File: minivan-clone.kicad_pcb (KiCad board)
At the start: 2 copper layers, 247.4 x 75.9 mm, 122 parts, among them CON101 HRO-TYPE-C-31-M-12, K101 KEYSW, K102 KEYSW, K103 KEYSW, K104 KEYSW, K105 KEYSW, K106 KEYSW, K107 KEYSW, K108 KEYSW, K109 KEYSW, K110 KEYSW, K111 KEYSW, K112 KEYSW, K113 KEYSW, K114 KEYSW, K115 KEYSW, K116 KEYSW, K118 KEYSW, K119 KEYSW, K120 KEYSW, K121 KEYSW, K122 KEYSW, K123 KEYSW, K124 KEYSW, K125 KEYSW, K126 KEYSW, K127 KEYSW, K128 KEYSW, K129 KEYSW, K130 KEYSW, K131 KEYSW, K132 KEYSW, K133 KEYSW, K134 KEYSW, K135 KEYSW, K136 KEYSW, K137 KEYSW, K138 KEYSW, K139 KEYSW, K140 KEYSW, K141 KEYSW, K142 KEYSW, K143 KEYSW, K144 KEYSW, K145 KEYSW, K146 KEYSW, K147 KEYSW, K148 KEYSW, SW101 SW_PUSH, U101 ATMEGA32U2, X101 XTAL_GND

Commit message: done with tracks for leftmost cols
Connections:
- >NAME pad 1: /PC4 -> /PD4
- D101 pad 1: /PB0 -> /PB6
- D102 pad 1: /PB0 -> /PB6
- D103 pad 1: /PB0 -> /PB6
- D104 pad 1: /PB0 -> /PB6
- D105 pad 1: /PB0 -> /PB6
- D106 pad 1: /PB0 -> /PB6
- D107 pad 1: /PB0 -> /PB6
- D108 pad 1: /PB0 -> /PB6
- D109 pad 1: /PB0 -> /PB6
- D110 pad 1: /PB0 -> /PB6
- D111 pad 1: /PB0 -> /PB6
- D112 pad 1: /PB0 -> /PB6
- D113 pad 1: /PB0 -> /PB6
- D114 pad 1: /PB1 -> /PB5
- D115 pad 1: /PB1 -> /PB5
- D116 pad 1: /PB1 -> /PB5
- D117 pad 1: /PB1 -> /PB5
- D118 pad 1: /PB1 -> /PB5
- D119 pad 1: /PB1 -> /PB5
- D120 pad 1: /PB1 -> /PB5
- D121 pad 1: /PB1 -> /PB5
- D122 pad 1: /PB1 -> /PB5
- D123 pad 1: /PB1 -> /PB5
- D124 pad 1: /PB1 -> /PB5
- D125 pad 1: /PB1 -> /PB5
- K101 pad 1: /PD6 -> /PC6
- K103 pad 1: /PD5 -> /PB7
- K104 pad 1: /PD4 -> /PC4
- K109 pad 1: /PB5 -> /PB1
- K110 pad 1: /PB6 -> /PB0
- K111 pad 1: /PC6 -> /PD6
- K112 pad 1: /PB7 -> /PD5
- K113 pad 1: /PC4 -> /PD4
- K115 pad 1: /PD5 -> /PB7
- K116 pad 1: /PD4 -> /PC4
- K122 pad 1: /PB5 -> /PB1
- K123 pad 1: /PB6 -> /PB0
- K124 pad 1: /PC6 -> /PD6
- K125 pad 1: /PB7 -> /PD5
- K126 pad 1: /PC4 -> /PD4
- K128 pad 1: /PD5 -> /PB7
- K129 pad 1: /PD4 -> /PC4
- K134 pad 1: /PB5 -> /PB1
- K135 pad 1: /PB6 -> /PB0
- K136 pad 1: /PC6 -> /PD6
- K137 pad 1: /PB7 -> /PD5
- K138 pad 1: /PC4 -> /PD4
- K139 pad 1: /PD5 -> /PB7
- K140 pad 1: /PD4 -> /PC4
- K145 pad 1: /PB5 -> /PB1
- K146 pad 1: /PB6 -> /PB0
- K147 pad 1: /PC6 -> /PD6
- K148 pad 1: /PB7 -> /PD5
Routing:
- net /PB5: track 48.0 -> 218.8 mm, vias 0 -> 2
- net /PD6: track 0.00 -> 162.0 mm, vias 0 -> 1
- net /PB6: track 103.0 -> 237.7 mm, vias 1 -> 2
- net /PC6: track 121.1 -> 0.00 mm, vias 1 -> 0
- net /PB1: track 218.8 -> 124.8 mm, vias 2 -> 1
- net /PB0: track 237.7 -> 144.7 mm, vias 2 -> 1
- net /PD4: track 91.1 -> 172.9 mm
- net /PD5: track 91.1 -> 170.6 mm, vias 0 -> 1
- net /PB2: track 48.0 -> 87.2 mm
- net /PC4: track 122.4 -> 91.1 mm
- net /PB7: track 107.0 -> 91.1 mm, vias 1 -> 0
- net Net-(D134-Pad2): track 0.00 -> 9.69 mm
- net Net-(D136-Pad2): track 0.00 -> 9.69 mm
- net Net-(D135-Pad2): track 0.00 -> 9.59 mm
- net Net-(D133-Pad2): track 0.00 -> 9.59 mm
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
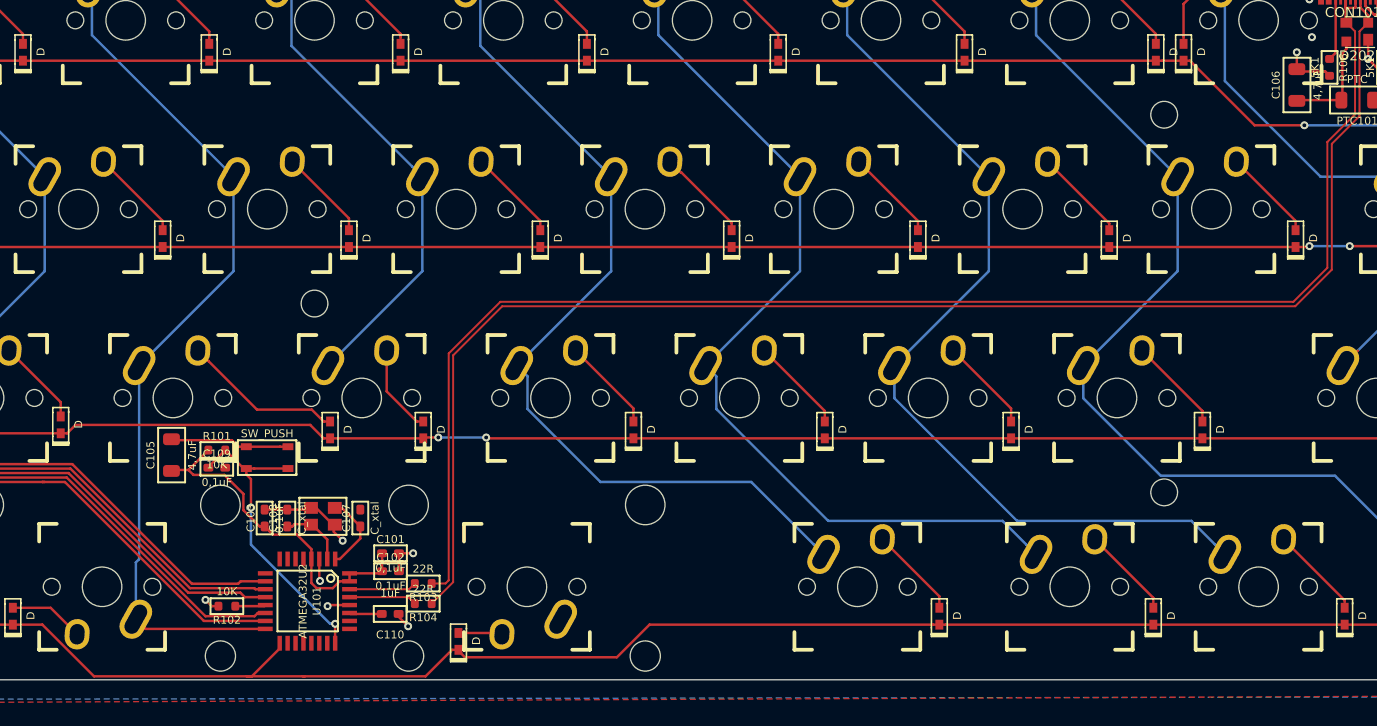
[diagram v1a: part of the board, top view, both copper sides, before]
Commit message: tracks for all leftmost rows, started with rightmost cols
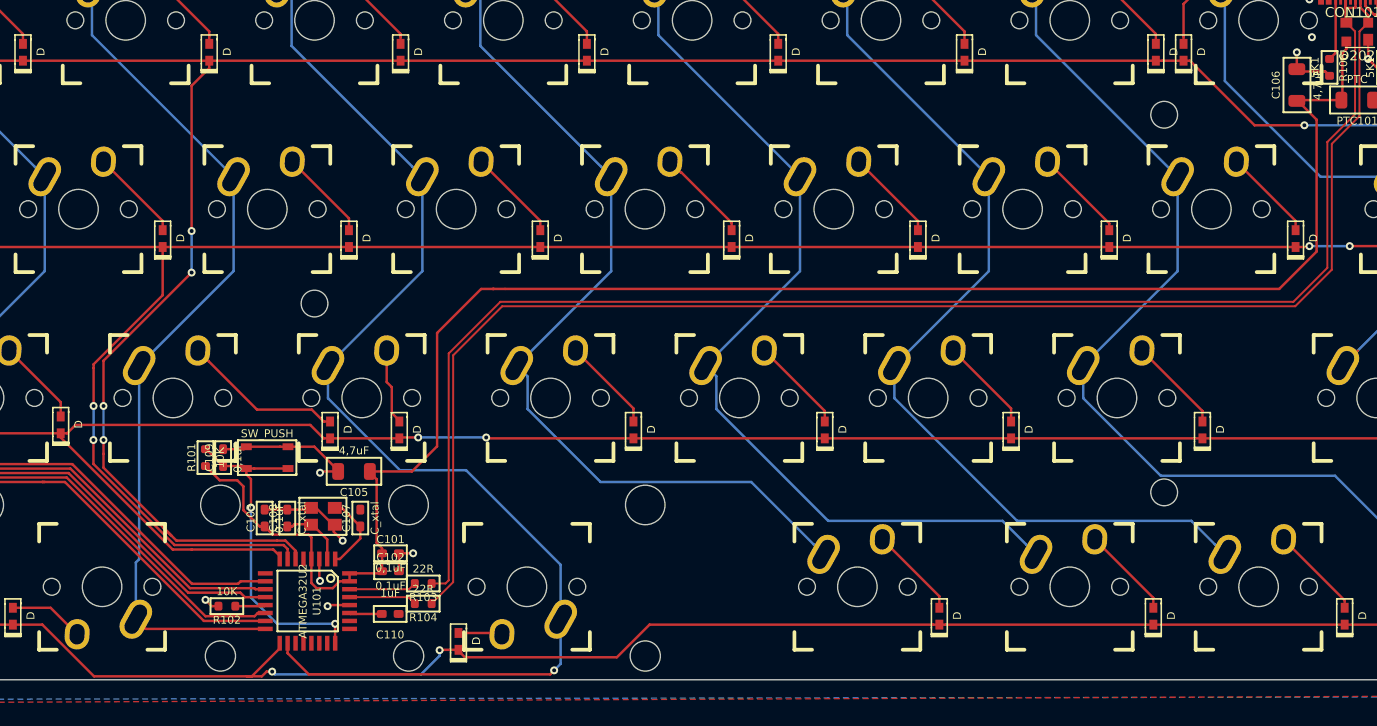
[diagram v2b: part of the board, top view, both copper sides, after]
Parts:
- moved C105 18.5 mm to (248.3, 183.5), turned to 180 degrees
- moved D132 2.41 mm to (252.9, 179.3)
- moved R101 1.37 mm to (233.3, 182.1), turned to 90 degrees
- moved C109 1.20 mm to (235.1, 182.1), turned to 90 degrees
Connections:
- D101 pad 1: /PB6 -> /PD0
- D102 pad 1: /PB6 -> /PD0
- D103 pad 1: /PB6 -> /PD0
- D104 pad 1: /PB6 -> /PD0
- D105 pad 1: /PB6 -> /PD0
- D106 pad 1: /PB6 -> /PD0
- D107 pad 1: /PB6 -> /PD0
- D108 pad 1: /PB6 -> /PD0
- D109 pad 1: /PB6 -> /PD0
- D110 pad 1: /PB6 -> /PD0
- D111 pad 1: /PB6 -> /PD0
- D112 pad 1: /PB6 -> /PD0
- D113 pad 1: /PB6 -> /PD0
- D114 pad 1: /PB5 -> /PD1
- D115 pad 1: /PB5 -> /PD1
- D116 pad 1: /PB5 -> /PD1
- D117 pad 1: /PB5 -> /PD1
- D118 pad 1: /PB5 -> /PD1
- D119 pad 1: /PB5 -> /PD1
- D120 pad 1: /PB5 -> /PD1
- D121 pad 1: /PB5 -> /PD1
- D122 pad 1: /PB5 -> /PD1
- D123 pad 1: /PB5 -> /PD1
- D124 pad 1: /PB5 -> /PD1
- D125 pad 1: /PB5 -> /PD1
- D126 pad 1: /PC2 -> /PD2
- D127 pad 1: /PC2 -> /PD2
- D128 pad 1: /PC2 -> /PD2
- D129 pad 1: /PC2 -> /PD2
- D130 pad 1: /PC2 -> /PD2
- D131 pad 1: /PC2 -> /PD2
- D132 pad 1: /PC2 -> /PD2
- D133 pad 1: /PC2 -> /PD2
- D134 pad 1: /PC2 -> /PD2
- D135 pad 1: /PC2 -> /PD2
- D136 pad 1: /PC2 -> /PD2
- D137 pad 1: /PC2 -> /PD2
- K102 pad 1: /PB4 -> /PB6
- K106 pad 1: /PD2 -> /PC2
- K107 pad 1: /PD0 -> /PB4
- K114 pad 1: /PB4 -> /PB6
- K119 pad 1: /PD2 -> /PC2
- K120 pad 1: /PD0 -> /PB4
- K127 pad 1: /PB4 -> /PB6
- K131 pad 1: /PD2 -> /PC2
- K132 pad 1: /PD0 -> /PB4
- K142 pad 1: /PD2 -> /PC2
- K143 pad 1: /PD0 -> /PB4
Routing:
- net /PD1: track 0.00 -> 267.7 mm, vias 0 -> 4
- net /PD0: track 48.0 -> 308.1 mm, vias 0 -> 6
- net /PB5: track 218.8 -> 0.00 mm, vias 2 -> 0
- net /PB6: track 237.7 -> 53.2 mm, vias 2 -> 0
- net /PD2: track 88.7 -> 248.2 mm, vias 0 -> 2
- net /PC2: track 220.4 -> 88.7 mm, vias 2 -> 0
- net +5V: track 45.7 -> 177.3 mm
- net /PB4: track 53.2 -> 121.6 mm, vias 0 -> 1
- net /RST: track 31.4 -> 34.4 mm
- net GND: track 46.2 -> 47.6 mm
- net Net-(D132-Pad2): track 9.07 -> 7.69 mm
- net /PB3: track 237.0 -> 237.4 mm, vias 0 -> 2

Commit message: added all tracks
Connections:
- K101 pad 1: /PC6 -> /PC7
- K102 pad 1: /PB6 -> /PC6
- K103 pad 1: /PB7 -> /PC4
- K104 pad 1: /PC4 -> /PC5
- K105 pad 1: /PD3 -> /PB6
- K106 pad 1: /PC2 -> /PB5
- K114 pad 1: /PB6 -> /PC6
- K115 pad 1: /PB7 -> /PC4
- K116 pad 1: /PC4 -> /PC5
- K118 pad 1: /PD3 -> /PB6
- K119 pad 1: /PC2 -> /PB5
- K127 pad 1: /PB6 -> /PC6
- K128 pad 1: /PB7 -> /PC4
- K129 pad 1: /PC4 -> /PC5
- K130 pad 1: /PD3 -> /PB6
- K131 pad 1: /PC2 -> /PB5
- K139 pad 1: /PB7 -> /PC4
- K140 pad 1: /PC4 -> /PC5
- K141 pad 1: /PD3 -> /PB6
- K142 pad 1: /PC2 -> /PB5
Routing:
- net /PC5: track 0.00 -> 188.2 mm, vias 0 -> 2
- net /PC7: track 0.00 -> 169.9 mm, vias 0 -> 3
- net /PC6: track 0.00 -> 169.0 mm, vias 0 -> 3
- net /PB5: track 0.00 -> 148.7 mm
- net /PB6: track 53.2 -> 176.8 mm, vias 0 -> 2
- net /PC4: track 91.1 -> 209.6 mm, vias 0 -> 2
- net /PD3: track 91.1 -> 0.00 mm
- net /PB7: track 91.1 -> 0.00 mm
- net /PC2: track 88.7 -> 0.00 mm
- net Net-(D101-Pad2): track 24.1 -> 21.8 mm

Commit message: fixed fills
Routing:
- net /PD6: track 162.0 -> 165.9 mm
- net /RST: track 34.4 -> 30.9 mm
- net /PC7: track 169.9 -> 170.9 mm

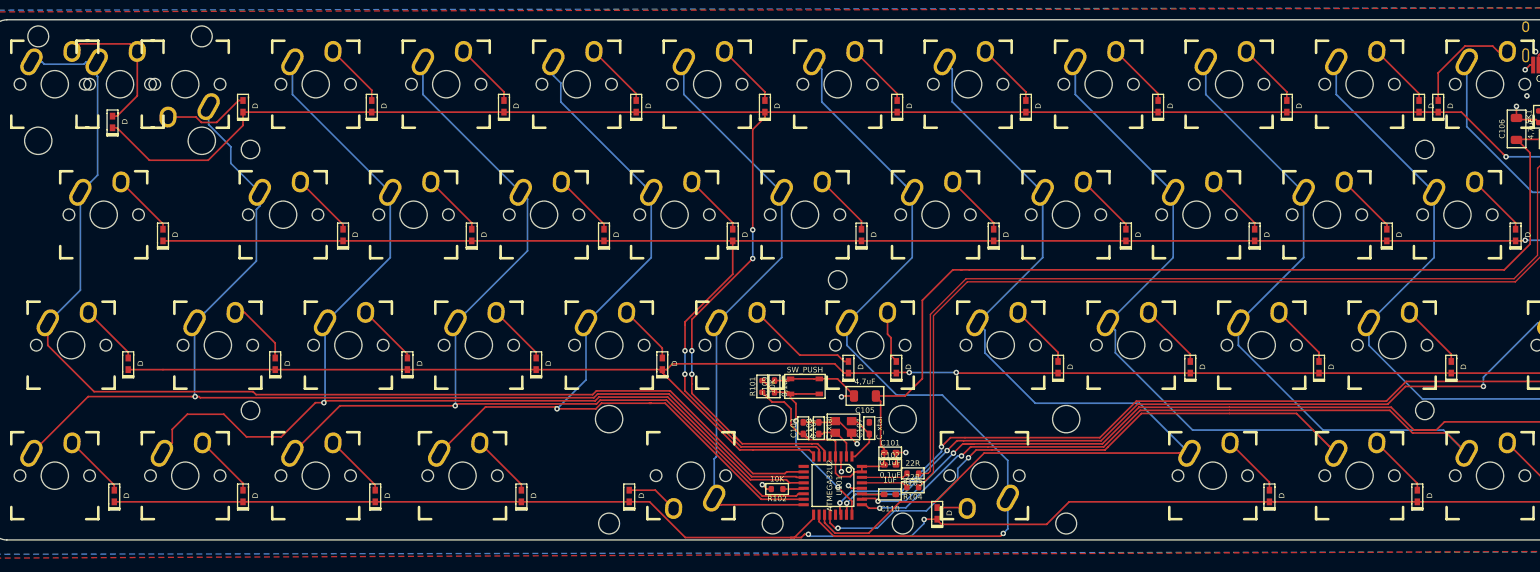
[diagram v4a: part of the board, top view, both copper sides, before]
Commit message: fixed DRC errors
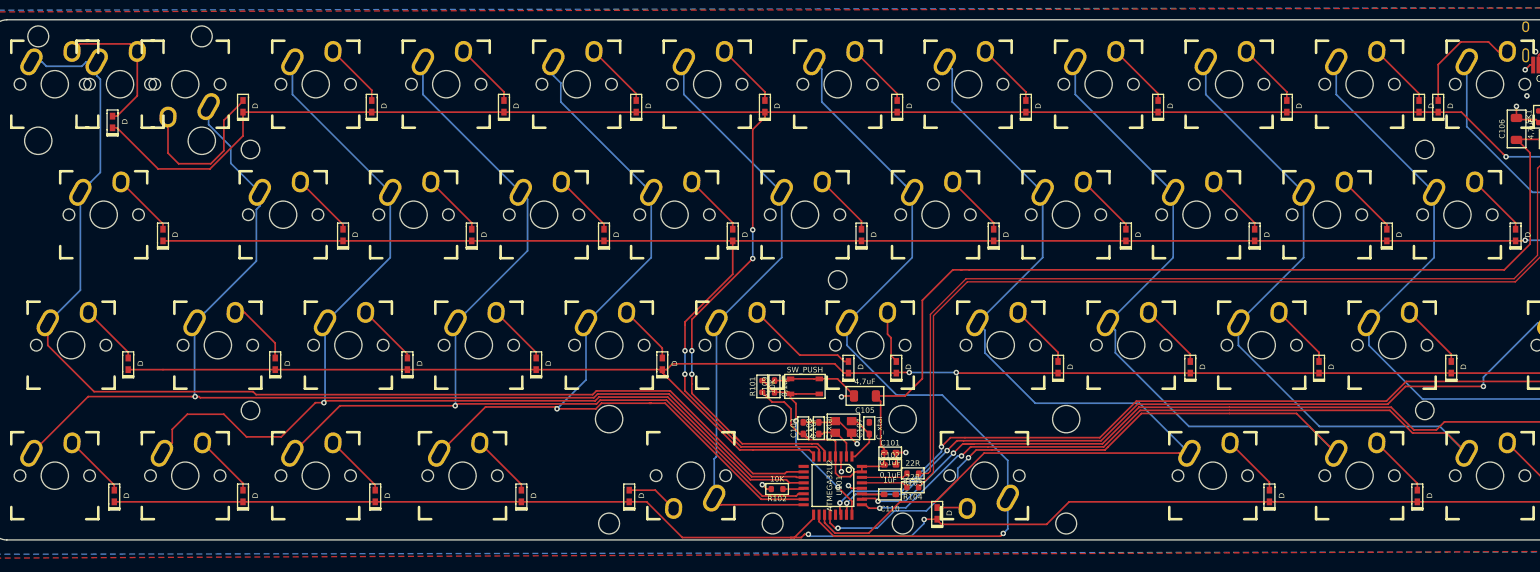
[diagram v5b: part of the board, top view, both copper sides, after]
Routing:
- net Net-(D102-Pad2): track 12.6 -> 23.3 mm
- net /PD0: track 308.1 -> 310.0 mm
- net Net-(D112-Pad2): track 16.1 -> 17.3 mm
- net /PD4: track 172.9 -> 173.5 mm

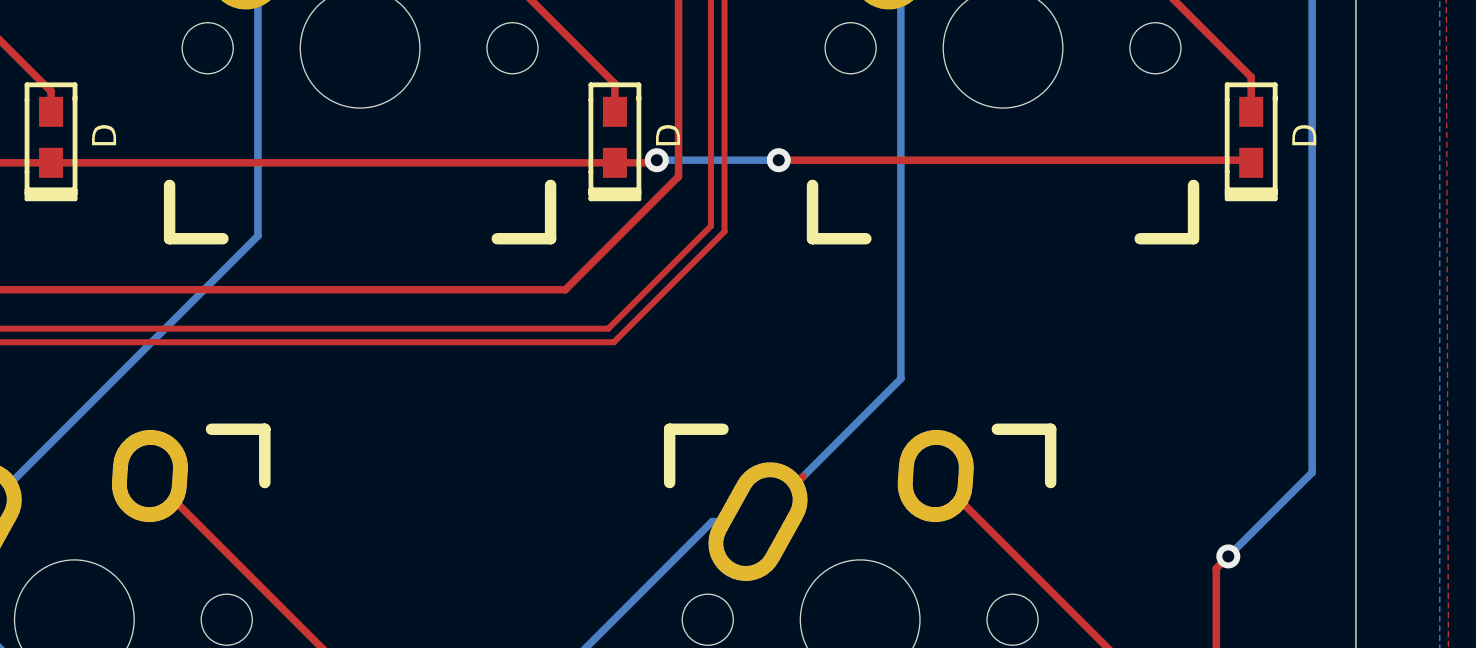
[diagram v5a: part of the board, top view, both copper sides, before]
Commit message: fixed logo in silk
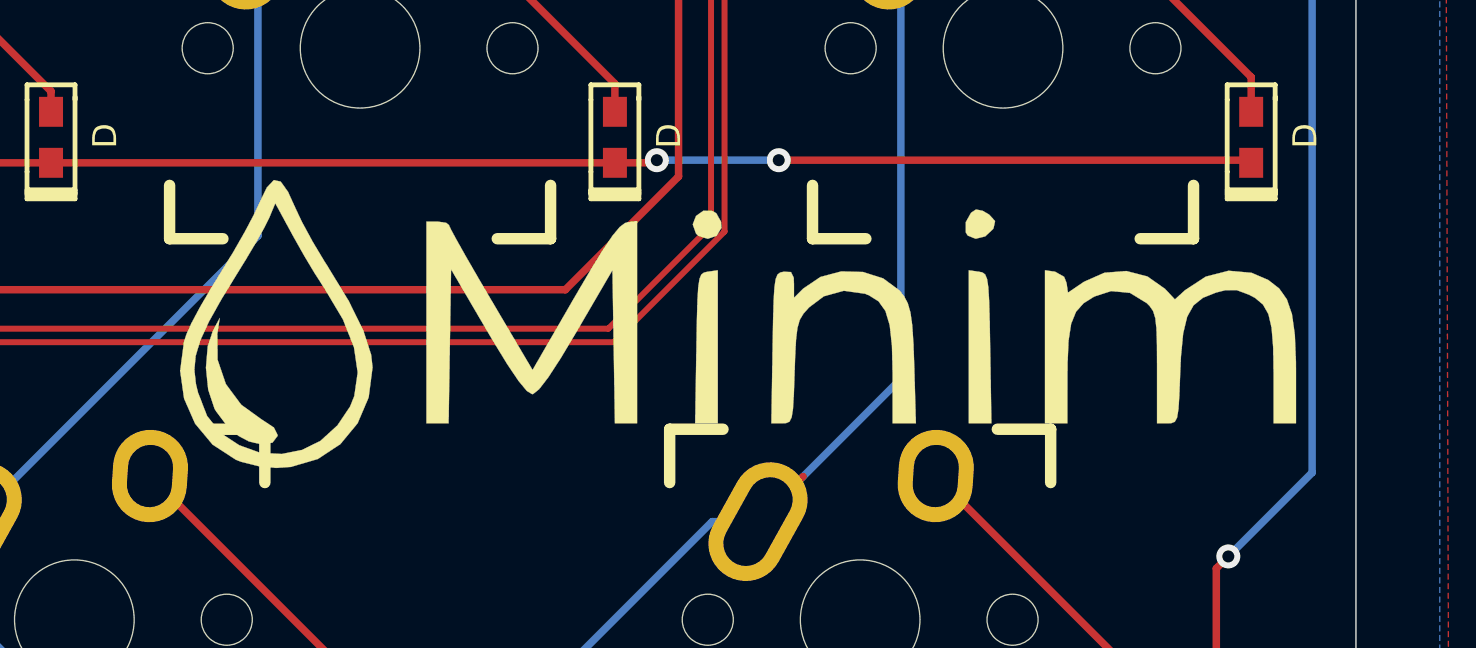
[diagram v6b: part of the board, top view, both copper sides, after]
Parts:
- moved G*** 2.05 mm to (346.7, 166.1)

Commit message: modified some footprints, removing outlines and references
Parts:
- moved D124 5.21 mm to (338.1, 160.0)
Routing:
- net /PD1: track 267.7 -> 281.3 mm
- net Net-(D124-Pad2): track 9.38 -> 0.00 mm
- net +5V: track 177.3 -> 176.1 mm

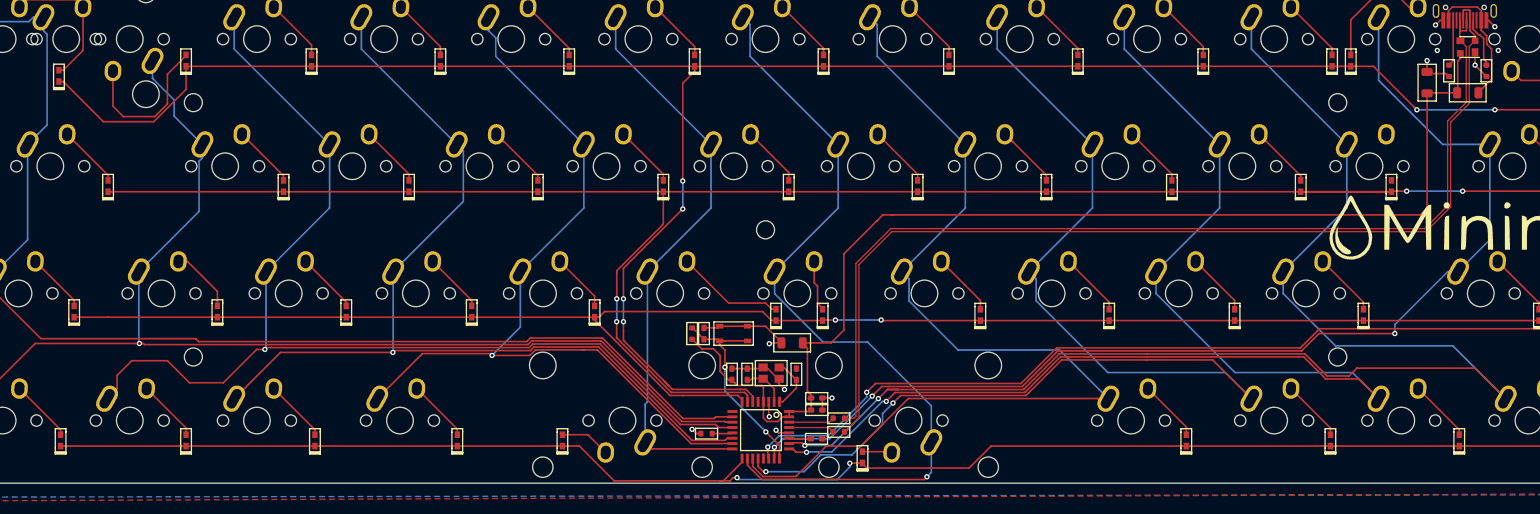
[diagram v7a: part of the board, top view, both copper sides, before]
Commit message: moved tracks at bottom of pcb, regenerated gerber
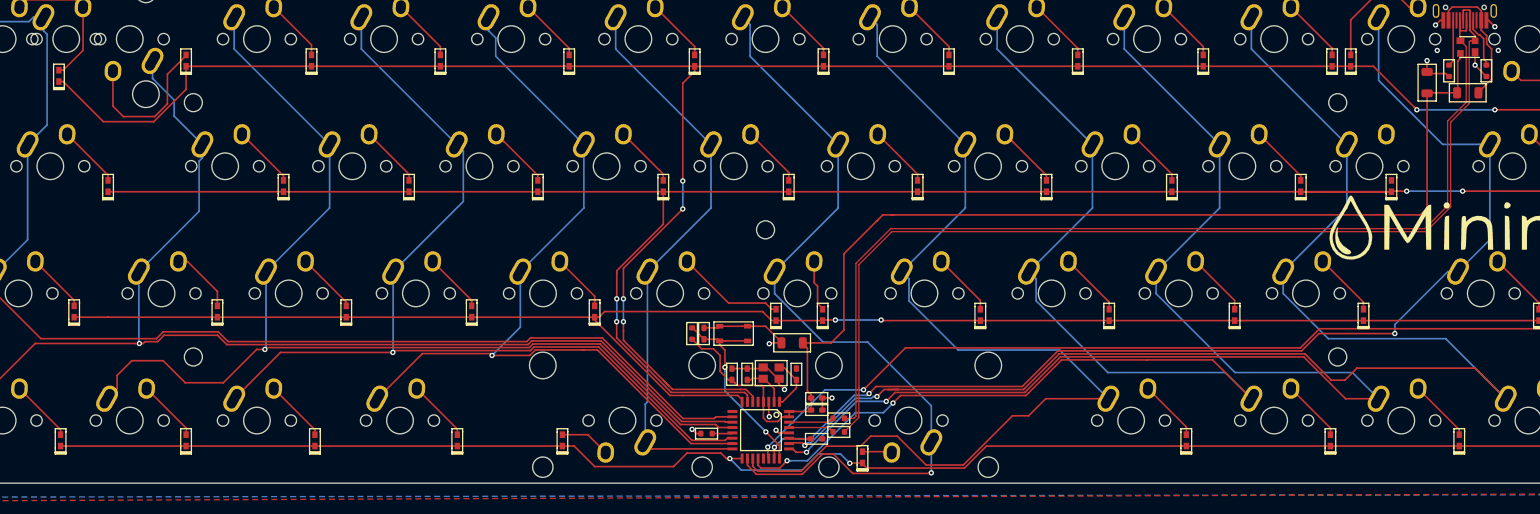
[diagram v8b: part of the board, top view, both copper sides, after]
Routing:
- net /PB5: track 148.7 -> 151.6 mm
- net /PB4: track 121.6 -> 123.3 mm
- net /PB3: track 237.4 -> 235.7 mm
- net /PB6: track 176.8 -> 175.3 mm
- net /PD5: track 170.9 -> 171.9 mm
- net /PD4: track 173.5 -> 174.4 mm
- net /PC4: track 209.6 -> 210.2 mm
